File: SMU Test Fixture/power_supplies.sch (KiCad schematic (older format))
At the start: 111 parts, among them J14 Conn_WallSocket_Earth, Q3 NJVMJB42CT4G, Q6 BCP56, T1 VPP12-4400, T2 VPP36-820, U10 LT3045xMSE-1, U11 LT3094xMSE, U9 MIC29510-5.0WT

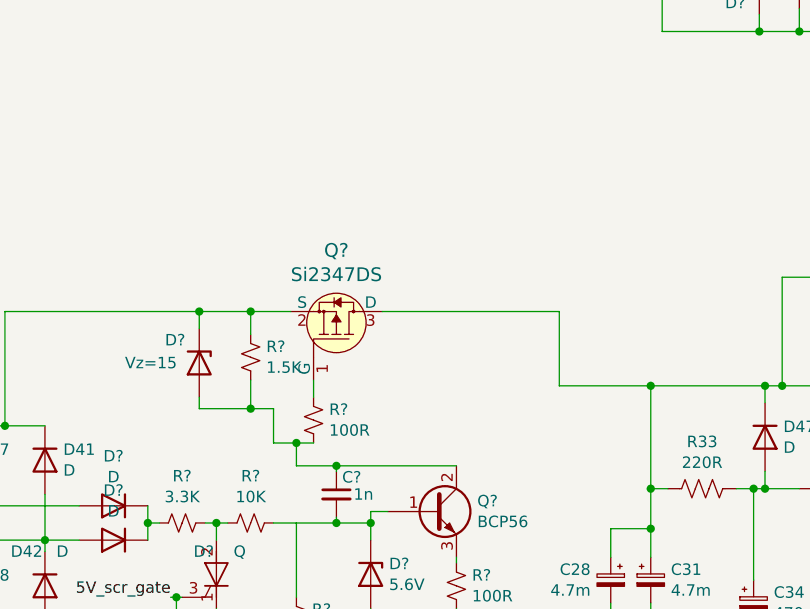
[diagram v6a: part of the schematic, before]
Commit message: parallel fet on 5v prereg
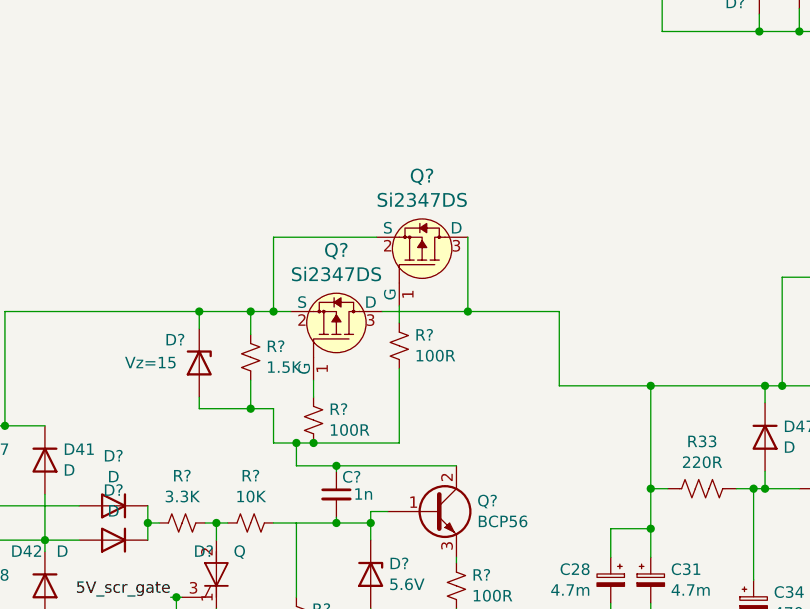
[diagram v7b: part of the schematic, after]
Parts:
- added Q?: Si2347DS, digikey-footprints:SOT-23-3, symbol dk_Transistors-FETs-MOSFETs-Single:DMG2305UX-13
- added R?: 100R, symbol Device:R_Small_US
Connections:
- net at D37.1 (K), D41.1 (K), D?.1 (K)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: now also Q?.2 (S)
- net at C28.1, C31.1, D47.1 (K)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: now also Q?.3 (D)
- net at C?.1, D?.2 (A), Q?.2 (C)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: now also R?.2
- new net: Q?.1 (G), R?.1
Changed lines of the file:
@@
 	4700 4725 4925 4725
 Wire Wire Line
-	4925 4725 5100 4725
+	4925 4725 5025 4725
 Connection ~ 4925 4725
 Wire Wire Line
@@
 Connection ~ 6675 6275
 Wire Wire Line
-	5500 4725 6275 4725
+	5500 4725 5875 4725
 Wire Wire Line
 	6275 4725 6275 5050
@@
 	6275 5050 6675 5050
 Connection ~ 6675 5050
+$Comp
+L dk_Transistors-FETs-MOSFETs-Single:DMG2305UX-13 Q?
+U 1 1 6324FA80
+P 5675 4400
+F 0 "Q?" V 5942 4400 60  0000 C CNN
+F 1 "Si2347DS" V 5836 4400 60  0000 C CNN
+F 2 "digikey-footprints:SOT-23-3" H 5875 4600 60  0001 L CNN
+F 3 "https://www.diodes.com/assets/Datasheets/DMG2305UX.pdf" H 5875 4700 60  0001 L CNN
+F 4 "DMG2305UX-13DICT-ND" H 5875 4800 60  0001 L CNN "Digi-Key_PN"
+F 5 "DMG2305UX-13" H 5875 4900 60  0001 L CNN "MPN"
+F 6 "Discrete Semiconductor Products" H 5875 5000 60  0001 L CNN "Category"
+F 7 "Transistors - FETs, MOSFETs - Single" H 5875 5100 60  0001 L CNN "Family"
+F 8 "https://www.diodes.com/assets/Datasheets/DMG2305UX.pdf" H 5875 5200 60  0001 L CNN "DK_Datasheet_Link"
+F 9 "/product-detail/en/diodes-incorporated/DMG2305UX-13/DMG2305UX-13DICT-ND/4251589" H 5875 5300 60  0001 L CNN "DK_Detail_Page"
+F 10 "MOSFET P-CH 20V 4.2A SOT23" H 5875 5400 60  0001 L CNN "Description"
+F 11 "Diodes Incorporated" H 5875 5500 60  0001 L CNN "Manufacturer"
+F 12 "Active" H 5875 5600 60  0001 L CNN "Status"
+	1    5675 4400
+	0    1    -1   0
+$EndComp
+Wire Wire Line
+	5575 4775 5575 4700
+$Comp
+L Device:R_Small_US R?
+U 1 1 6324FA87
+P 5575 4875
+F 0 "R?" H 5643 4921 50  0000 L CNN
+F 1 "100R" H 5643 4830 50  0000 L CNN
+F 2 "" H 5575 4875 50  0001 C CNN
+F 3 "~" H 5575 4875 50  0001 C CNN
+	1    5575 4875
+	1    0    0    -1
+$EndComp
+Wire Wire Line
+	5475 4400 5025 4400
+Wire Wire Line
+	5025 4400 5025 4725
+Connection ~ 5025 4725
+Wire Wire Line
+	5025 4725 5100 4725
+Wire Wire Line
+	5875 4400 5875 4725
+Connection ~ 5875 4725
+Wire Wire Line
+	5875 4725 6275 4725
+Wire Wire Line
+	5575 4975 5575 5300
+Wire Wire Line
+	5575 5300 5200 5300
+Connection ~ 5200 5300
 $EndSCHEMATC

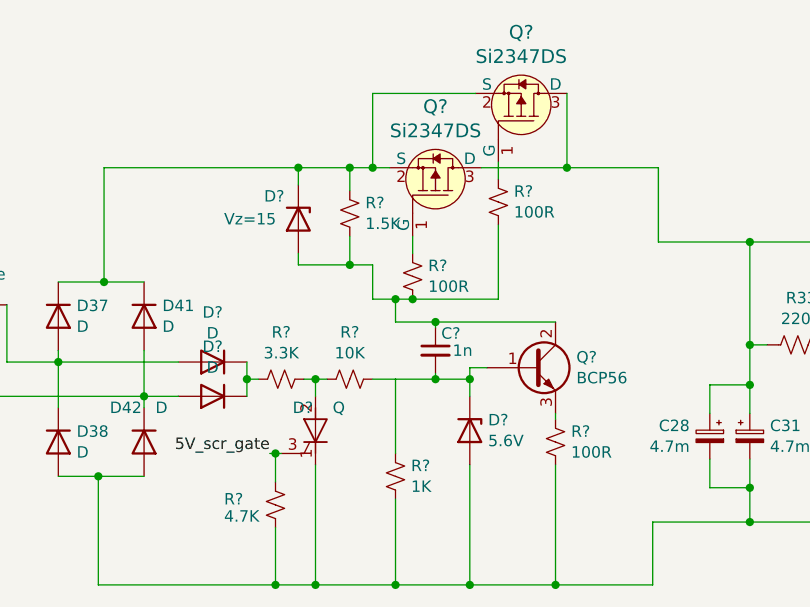
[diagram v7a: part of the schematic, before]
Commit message: Add simulations and relay state spreadsheet
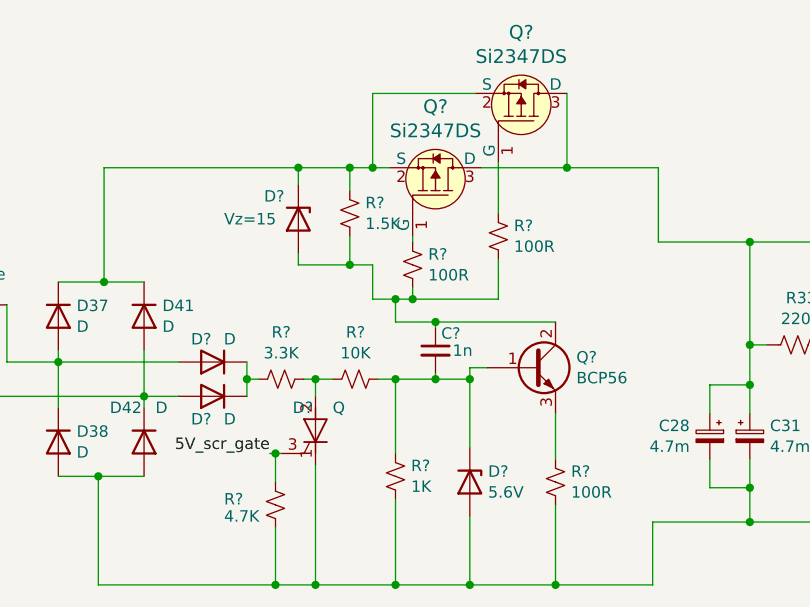
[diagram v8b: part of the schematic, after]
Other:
- moved on the sheet: D?, R?
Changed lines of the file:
@@
 $EndComp
 Wire Wire Line
-	5200 5100 5200 5025
+	5200 5050 5200 5025
 $Comp
 L Device:R_Small_US R?
 U 1 1 626368BA
-P 5200 5200
-F 0 "R?" H 5268 5246 50  0000 L CNN
-F 1 "100R" H 5268 5155 50  0000 L CNN
-F 2 "" H 5200 5200 50  0001 C CNN
-F 3 "~" H 5200 5200 50  0001 C CNN
-	1    5200 5200
+P 5200 5150
+F 0 "R?" H 5268 5196 50  0000 L CNN
+F 1 "100R" H 5268 5105 50  0000 L CNN
+F 2 "" H 5200 5150 50  0001 C CNN
+F 3 "~" H 5200 5150 50  0001 C CNN
+	1    5200 5150
 	1    0    0    -1
 $EndComp
@@
 U 1 1 62A1AA71
 P 4325 5575
-F 0 "D?" H 4325 5358 50  0000 C CNN
-F 1 "D" H 4325 5449 50  0000 C CNN
+F 0 "D?" H 4375 5475 50  0000 C CNN
+F 1 "D" H 4250 5475 50  0000 C CNN
 F 2 "" H 4325 5575 50  0001 C CNN
 F 3 "~" H 4325 5575 50  0001 C CNN
@@
 U 1 1 62A1C018
 P 4325 5725
-F 0 "D?" H 4325 5508 50  0000 C CNN
-F 1 "D" H 4325 5599 50  0000 C CNN
+F 0 "D?" H 4375 5825 50  0000 C CNN
+F 1 "D" H 4250 5825 50  0000 C CNN
 F 2 "" H 4325 5725 50  0001 C CNN
 F 3 "~" H 4325 5725 50  0001 C CNN
@@
 L Device:R_Small_US R?
 U 1 1 62AD6BD3
-P 4925 5650
-F 0 "R?" V 4720 5650 50  0000 C CNN
-F 1 "10K" V 4811 5650 50  0000 C CNN
-F 2 "" H 4925 5650 50  0001 C CNN
-F 3 "~" H 4925 5650 50  0001 C CNN
-	1    4925 5650
+P 4950 5650
+F 0 "R?" V 4745 5650 50  0000 C CNN
+F 1 "10K" V 4836 5650 50  0000 C CNN
+F 2 "" H 4950 5650 50  0001 C CNN
+F 3 "~" H 4950 5650 50  0001 C CNN
+	1    4950 5650
 	0    1    1    0
 $EndComp
@@
 	4775 5650 4725 5650
 Wire Wire Line
-	4775 5650 4825 5650
+	4775 5650 4850 5650
 Connection ~ 4775 5650
 $Comp
@@
 	5125 5975 5125 5650
 Wire Wire Line
-	5125 5650 5025 5650
+	5125 5650 5050 5650
 Wire Wire Line
 	5125 6175 5125 6550
@@
 L Device:R_Small_US R?
 U 1 1 62CEA686
-P 5825 5925
-F 0 "R?" H 5893 5971 50  0000 L CNN
-F 1 "100R" H 5893 5880 50  0000 L CNN
-F 2 "" H 5825 5925 50  0001 C CNN
-F 3 "~" H 5825 5925 50  0001 C CNN
-	1    5825 5925
-	1    0    0    -1
-$EndComp
-Wire Wire Line
-	5825 6025 5825 6550
+P 5825 6100
+F 0 "R?" H 5893 6146 50  0000 L CNN
+F 1 "100R" H 5893 6055 50  0000 L CNN
+F 2 "" H 5825 6100 50  0001 C CNN
+F 3 "~" H 5825 6100 50  0001 C CNN
+	1    5825 6100
+	1    0    0    -1
+$EndComp
+Wire Wire Line
+	5825 6200 5825 6550
 $Comp
 L Transistor_BJT:BCP56 Q?
@@
 $EndComp
 Wire Wire Line
-	5825 5800 5825 5825
+	5825 5800 5825 6000
 $Comp
 L Device:D_Zener D?
 U 1 1 62CEA694
-P 5450 5875
-F 0 "D?" V 5404 5955 50  0000 L CNN
-F 1 "5.6V" V 5495 5955 50  0000 L CNN
-F 2 "" H 5450 5875 50  0001 C CNN
-F 3 "~" H 5450 5875 50  0001 C CNN
-	1    5450 5875
+P 5450 6100
+F 0 "D?" V 5404 6180 50  0000 L CNN
+F 1 "5.6V" V 5495 6180 50  0000 L CNN
+F 2 "" H 5450 6100 50  0001 C CNN
+F 3 "~" H 5450 6100 50  0001 C CNN
+	1    5450 6100
 	0    1    1    0
 $EndComp
 Wire Wire Line
-	5450 6025 5450 6550
-Wire Wire Line
-	5450 5725 5450 5650
+	5450 6250 5450 6550
+Wire Wire Line
+	5450 5950 5450 5650
 $Comp
 L Device:C_Small C?
@@
 Wire Wire Line
 	5125 5300 5125 5400
-Connection ~ 5125 5300
-Wire Wire Line
-	5125 5300 5200 5300
 Wire Wire Line
 	5125 6550 5450 6550
@@
 $EndComp
 Wire Wire Line
-	5575 4775 5575 4700
+	5575 4925 5575 4700
 $Comp
 L Device:R_Small_US R?
 U 1 1 6324FA87
-P 5575 4875
-F 0 "R?" H 5643 4921 50  0000 L CNN
-F 1 "100R" H 5643 4830 50  0000 L CNN
-F 2 "" H 5575 4875 50  0001 C CNN
-F 3 "~" H 5575 4875 50  0001 C CNN
-	1    5575 4875
+P 5575 5025
+F 0 "R?" H 5643 5071 50  0000 L CNN
+F 1 "100R" H 5643 4980 50  0000 L CNN
+F 2 "" H 5575 5025 50  0001 C CNN
+F 3 "~" H 5575 5025 50  0001 C CNN
+	1    5575 5025
 	1    0    0    -1
 $EndComp
@@
 	5875 4725 6275 4725
 Wire Wire Line
-	5575 4975 5575 5300
-Wire Wire Line
-	5575 5300 5200 5300
+	5575 5125 5575 5300
+Wire Wire Line
+	5200 5250 5200 5300
+Wire Wire Line
+	5200 5300 5125 5300
+Connection ~ 5125 5300
+Wire Wire Line
+	5200 5300 5575 5300
 Connection ~ 5200 5300
+Connection ~ 5125 5650
 $EndSCHEMATC
